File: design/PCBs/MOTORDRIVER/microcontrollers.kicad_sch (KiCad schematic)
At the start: 19 parts, among them IC1 ATSAME53J18A-MF, U11 ATSAMD11D14A-M

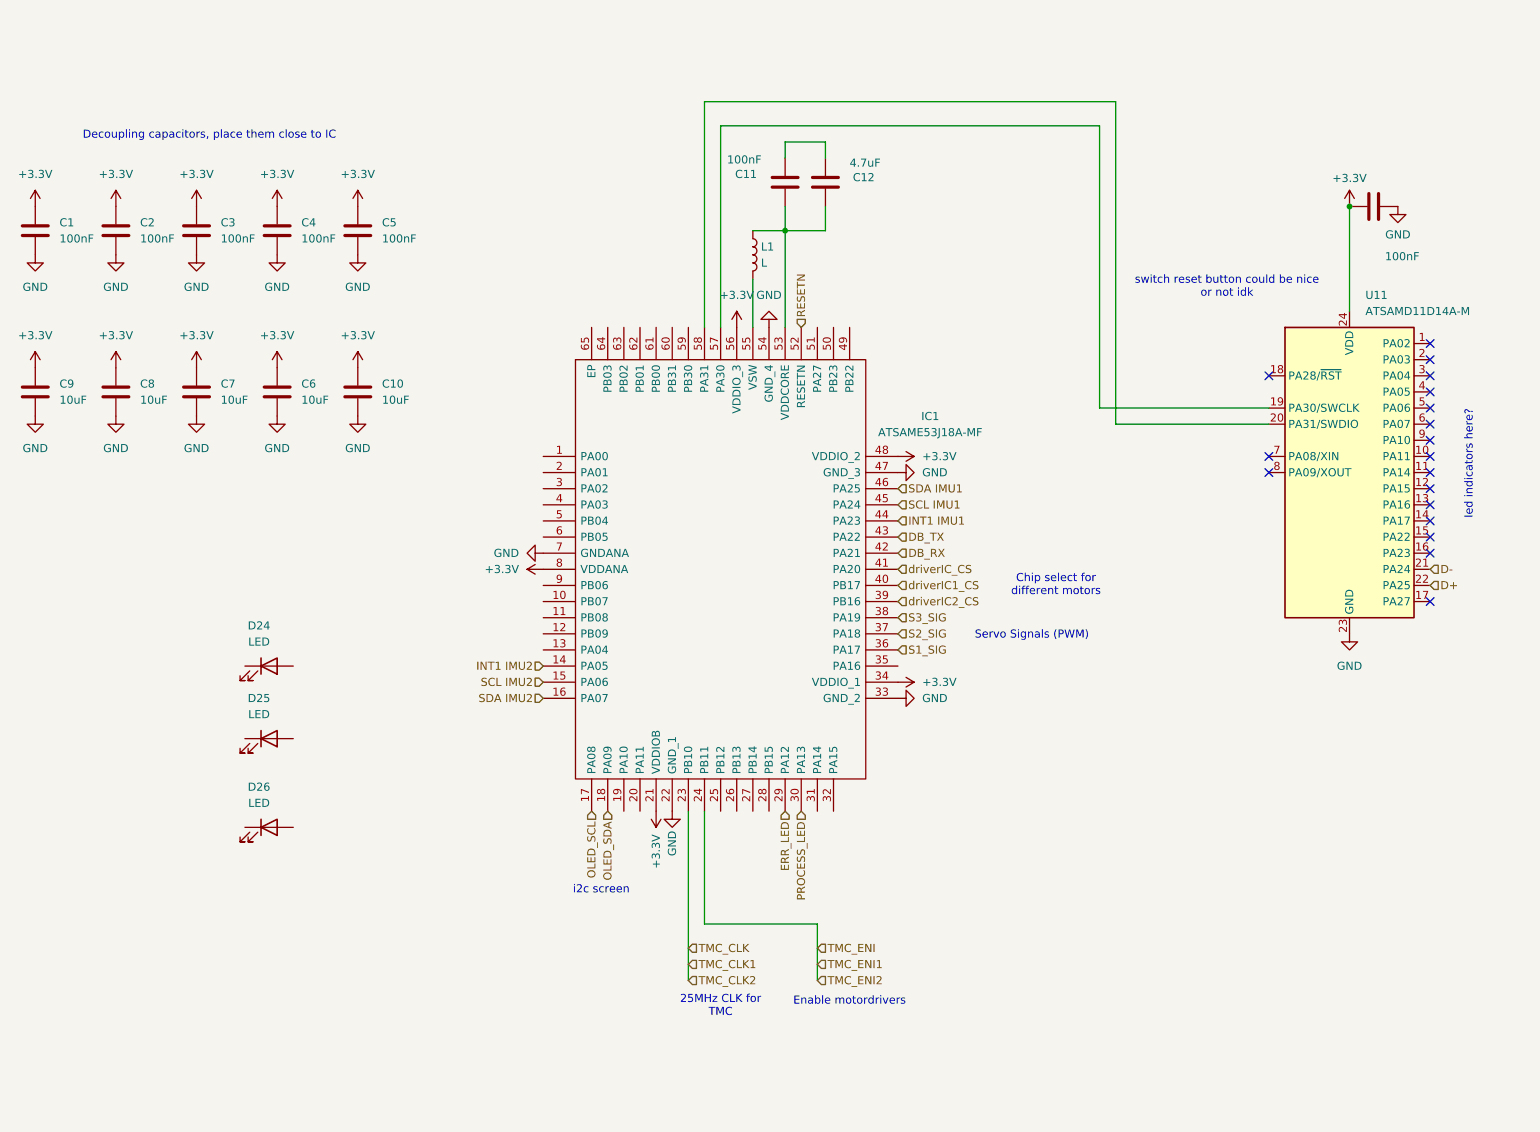
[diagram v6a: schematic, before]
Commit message: documentation, values, double-checking stuff
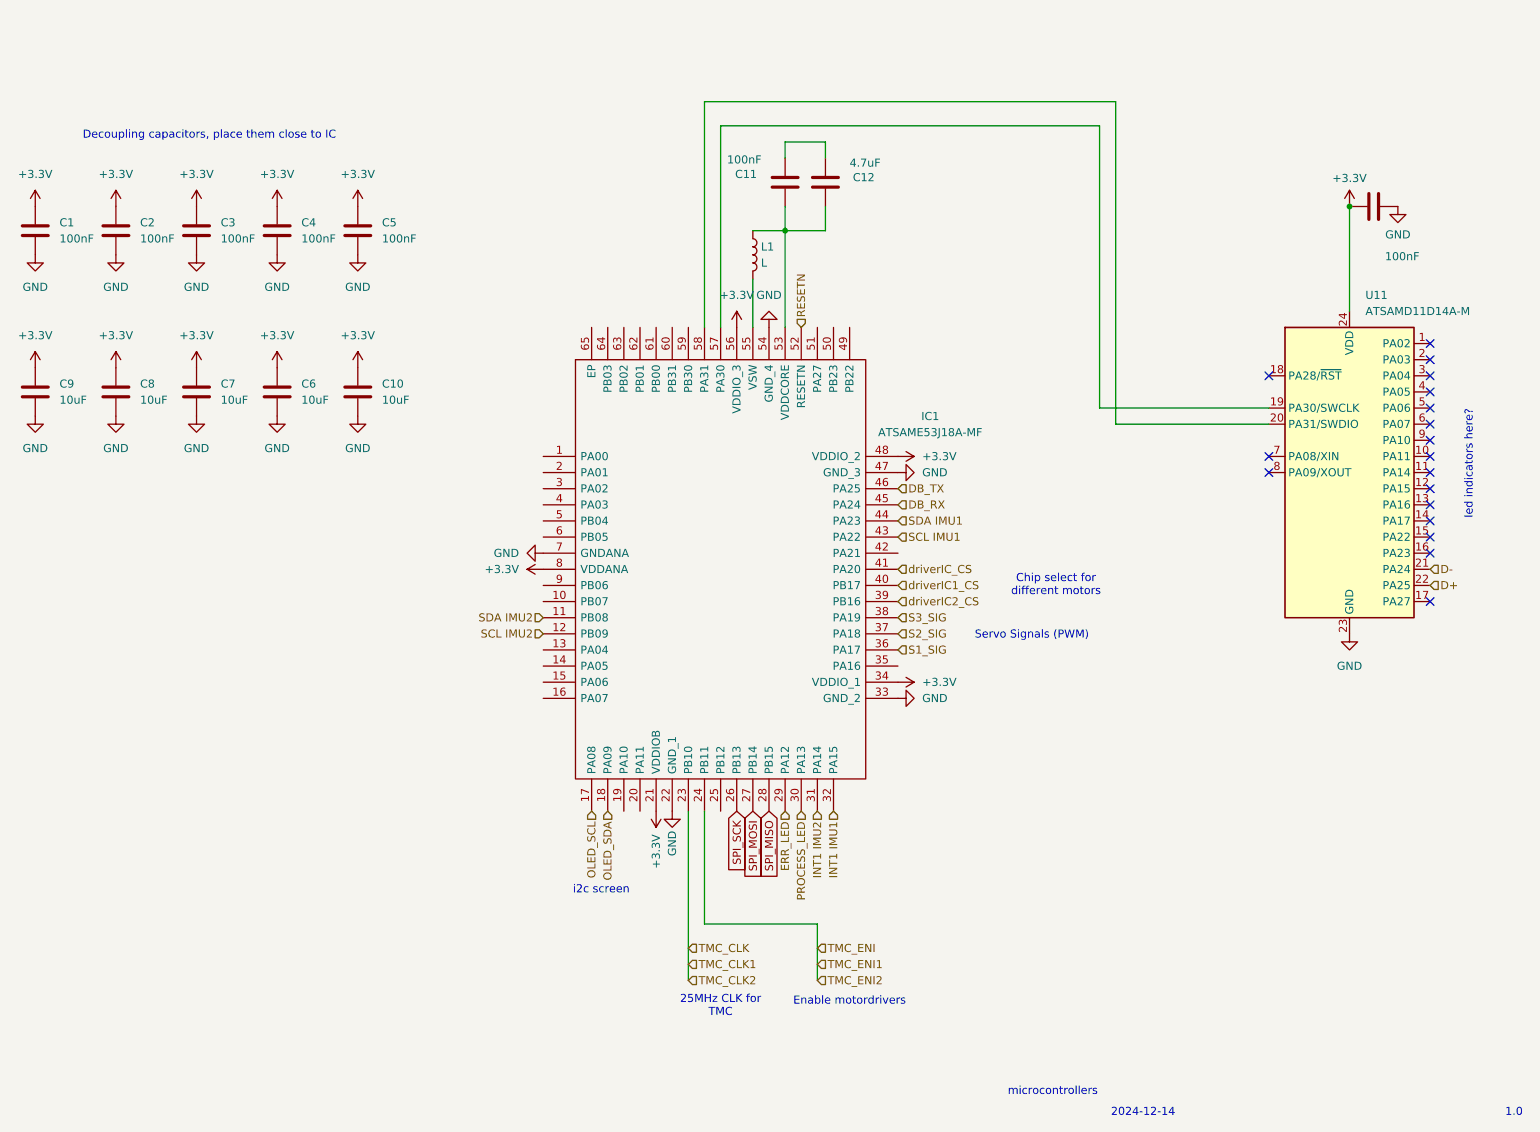
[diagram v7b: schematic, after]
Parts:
- removed D24, D25, D26: LED, symbol Device:LED
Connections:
- net DB_RX: now also IC1.45 (PA24); no longer IC1.42 (PA21)
- net DB_TX: now also IC1.46 (PA25); no longer IC1.43 (PA22)
- net INT1 IMU1: now also IC1.32 (PA15); no longer IC1.44 (PA23)
- net INT1 IMU2: now also IC1.31 (PA14); no longer IC1.14 (PA05)
- net SCL IMU1: now also IC1.43 (PA22); no longer IC1.45 (PA24)
- net SCL IMU2: now also IC1.12 (PB09); no longer IC1.15 (PA06)
- net SDA IMU1: now also IC1.44 (PA23); no longer IC1.46 (PA25)
- net SDA IMU2: now also IC1.11 (PB08); no longer IC1.16 (PA07)
- net SPI_SCK: now reaches IC1.26 (PB13)
- net SPI_MOSI: now reaches IC1.27 (PB14)
- net SPI_MISO: now reaches IC1.28 (PB15)
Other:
- note added: "1.0"
- note added: "2024-12-14"
- note added: "microcontrollers"
- note removed: "switch reset button could be nice or not idk"
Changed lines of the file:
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@@
 		)
 	)
+	(text "1.0"
+		(exclude_from_sim no)
+		(at 271.018 193.548 0)
+		(effects
+			(font
+				(size 1.27 1.27)
+			)
+		)
+	)
 	(text "Chip select for\ndifferent motors\n"
 		(exclude_from_sim no)
@@
 		)
 	)
-	(text "i2c screen"
+	(text "microcontrollers\n"
 		(exclude_from_sim no)
-		(at 127.254 158.496 0)
+		(at 198.374 190.246 0)
 		(effects
 			(font
@@
 		)
 	)
-	(text "switch reset button could be nice\nor not idk\n"
+	(text "i2c screen"
 		(exclude_from_sim no)
-		(at 225.806 63.5 0)
+		(at 127.254 158.496 0)
 		(effects
 			(font
@@
 		)
 	)
+	(text "2024-12-14"
+		(exclude_from_sim no)
+		(at 212.598 193.548 0)
+		(effects
+			(font
+				(size 1.27 1.27)
+			)
+		)
+	)
 	(text "Enable motordrivers"
 		(exclude_from_sim no)
@@
 		)
 	)
+	(global_label "SPI_MISO"
+		(shape input)
+		(at 153.67 146.05 270)
+		(fields_autoplaced yes)
+		(effects
+			(font
+				(size 1.27 1.27)
+			)
+			(justify right)
+		)
+		(property "Intersheetrefs" "${INTERSHEET_REFS}"
+			(at 153.67 157.3491 90)
+			(effects
+				(font
+					(size 1.27 1.27)
+				)
+				(justify right)
+				(hide yes)
+			)
+		)
+	)
+	(global_label "SPI_SCK"
+		(shape input)
+		(at 148.59 146.05 270)
+		(fields_autoplaced yes)
+		(effects
+			(font
+				(size 1.27 1.27)
+			)
+			(justify right)
+		)
+		(property "Intersheetrefs" "${INTERSHEET_REFS}"
+			(at 148.59 156.2821 90)
+			(effects
+				(font
+					(size 1.27 1.27)
+				)
+				(justify right)
+				(hide yes)
+			)
+		)
+	)
+	(global_label "SPI_MOSI"
+		(shape input)
+		(at 151.13 146.05 270)
+		(fields_autoplaced yes)
+		(effects
+			(font
+				(size 1.27 1.27)
+			)
+			(justify right)
+		)
+		(property "Intersheetrefs" "${INTERSHEET_REFS}"
+			(at 151.13 157.3491 90)
+			(effects
+				(font
+					(size 1.27 1.27)
+				)
+				(justify right)
+				(hide yes)
+			)
+		)
+	)
 	(hierarchical_label "driverIC2_CS"
 		(shape input)
@@
 	(hierarchical_label "SDA IMU1"
 		(shape input)
-		(at 173.99 95.25 0)
+		(at 173.99 100.33 0)
 		(fields_autoplaced yes)
 		(effects
@@
 	(hierarchical_label "DB_RX"
 		(shape input)
-		(at 173.99 105.41 0)
+		(at 173.99 97.79 0)
 		(fields_autoplaced yes)
 		(effects
@@
 	(hierarchical_label "DB_TX"
 		(shape input)
-		(at 173.99 102.87 0)
+		(at 173.99 95.25 0)
 		(fields_autoplaced yes)
 		(effects
@@
 	(hierarchical_label "SDA IMU2"
 		(shape input)
-		(at 118.11 128.27 180)
+		(at 118.11 115.57 180)
 		(fields_autoplaced yes)
 		(effects
@@
 	(hierarchical_label "SCL IMU2"
 		(shape input)
-		(at 118.11 125.73 180)
+		(at 118.11 118.11 180)
 		(fields_autoplaced yes)
 		(effects
@@
 	(hierarchical_label "SCL IMU1"
 		(shape input)
-		(at 173.99 97.79 0)
+		(at 173.99 102.87 0)
 		(fields_autoplaced yes)
 		(effects
@@
 	(hierarchical_label "INT1 IMU2"
 		(shape input)
-		(at 118.11 123.19 180)
+		(at 161.29 146.05 270)
 		(fields_autoplaced yes)
 		(effects
@@
 	(hierarchical_label "INT1 IMU1"
 		(shape input)
-		(at 173.99 100.33 0)
+		(at 163.83 146.05 270)
 		(fields_autoplaced yes)
 		(effects
@@
 				(size 1.27 1.27)
 			)
-			(justify left)
+			(justify right)
 		)
 	)
@@
 	)
 	(symbol
-		(lib_id "Device:LED")
-		(at 74.93 148.59 0)
-		(unit 1)
-		(exclude_from_sim no)
-		(in_bom yes)
-		(on_board yes)
-		(dnp no)
-		(fields_autoplaced yes)
-		(property "Reference" "D26"
-			(at 73.3425 142.24 0)
-			(effects
-				(font
-					(size 1.27 1.27)
-				)
-			)
-		)
-		(property "Value" "LED"
-			(at 73.3425 144.78 0)
-			(effects
-				(font
-					(size 1.27 1.27)
-				)
-			)
-		)
-		(property "Footprint" ""
-			(at 74.93 148.59 0)
-			(effects
-				(font
-					(size 1.27 1.27)
-				)
-				(hide yes)
-			)
-		)
-		(property "Datasheet" "~"
-			(at 74.93 148.59 0)
-			(effects
-				(font
-					(size 1.27 1.27)
-				)
-				(hide yes)
-			)
-		)
-		(property "Description" "Light emitting diode"
-			(at 74.93 148.59 0)
-			(effects
-				(font
-					(size 1.27 1.27)
-				)
-				(hide yes)
-			)
-		)
-		(pin "1"
-		)
-		(pin "2"
-		)
-		(instances
-			(project "motordriver"
-				(path "/c7634e88-16d1-45ec-9aac-9c841e03cf6d/9ebbb593-eaf1-4a56-ba2a-164e20b1d55e"
-					(reference "D26")
-					(unit 1)
-				)
-			)
-		)
-	)
-	(symbol
 		(lib_id "power:GND")
 		(at 63.5 83.82 0)
@@
 	)
 	(symbol
-		(lib_id "Device:LED")
-		(at 74.93 134.62 0)
-		(unit 1)
-		(exclude_from_sim no)
-		(in_bom yes)
-		(on_board yes)
-		(dnp no)
-		(fields_autoplaced yes)
-		(property "Reference" "D25"
-			(at 73.3425 128.27 0)
-			(effects
-				(font
-					(size 1.27 1.27)
-				)
-			)
-		)
-		(property "Value" "LED"
-			(at 73.3425 130.81 0)
-			(effects
-				(font
-					(size 1.27 1.27)
-				)
-			)
-		)
-		(property "Footprint" ""
-			(at 74.93 134.62 0)
-			(effects
-				(font
-					(size 1.27 1.27)
-				)
-				(hide yes)
-			)
-		)
-		(property "Datasheet" "~"
-			(at 74.93 134.62 0)
-			(effects
-				(font
-					(size 1.27 1.27)
-				)
-				(hide yes)
-			)
-		)
-		(property "Description" "Light emitting diode"
-			(at 74.93 134.62 0)
-			(effects
-				(font
-					(size 1.27 1.27)
-				)
-				(hide yes)
-			)
-		)
-		(pin "1"
-		)
-		(pin "2"
-		)
-		(instances
-			(project "motordriver"
-				(path "/c7634e88-16d1-45ec-9aac-9c841e03cf6d/9ebbb593-eaf1-4a56-ba2a-164e20b1d55e"
-					(reference "D25")
-					(unit 1)
-				)
-			)
-		)
-	)
-	(symbol
 		(lib_id "power:+3.3V")
 		(at 76.2 50.8 0)
@@
 					(unit 1)
 				)
-			)
-		)
-	)
-	(symbol
-		(lib_id "Device:LED")
-		(at 74.93 123.19 0)
-		(unit 1)
-		(exclude_from_sim no)
-		(in_bom yes)
-		(on_board yes)
-		(dnp no)
-		(fields_autoplaced yes)
-		(property "Reference" "D24"
-			(at 73.3425 116.84 0)
-			(effects
-				(font
-					(size 1.27 1.27)
-				)
-			)
-		)
-		(property "Value" "LED"
-			(at 73.3425 119.38 0)
-			(effects
-				(font
-					(size 1.27 1.27)
-				)
-			)
-		)
-		(property "Footprint" ""
-			(at 74.93 123.19 0)
-			(effects
-				(font
-					(size 1.27 1.27)
-				)
-				(hide yes)
-			)
-		)
-		(property "Datasheet" "~"
-			(at 74.93 123.19 0)
-			(effects
-				(font
-					(size 1.27 1.27)
-				)
-				(hide yes)
-			)
-		)
-		(property "Description" "Light emitting diode"
-			(at 74.93 123.19 0)
-			(effects
-				(font
-					(size 1.27 1.27)
-				)
-				(hide yes)
-			)
-		)
-		(pin "1"
-		)
-		(pin "2"
-		)
-		(instances
-			(project ""
-				(path "/c7634e88-16d1-45ec-9aac-9c841e03cf6d/9ebbb593-eaf1-4a56-ba2a-164e20b1d55e"
-					(reference "D24")
-					(unit 1)
-				)

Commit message: cleaned up, added values and footprints
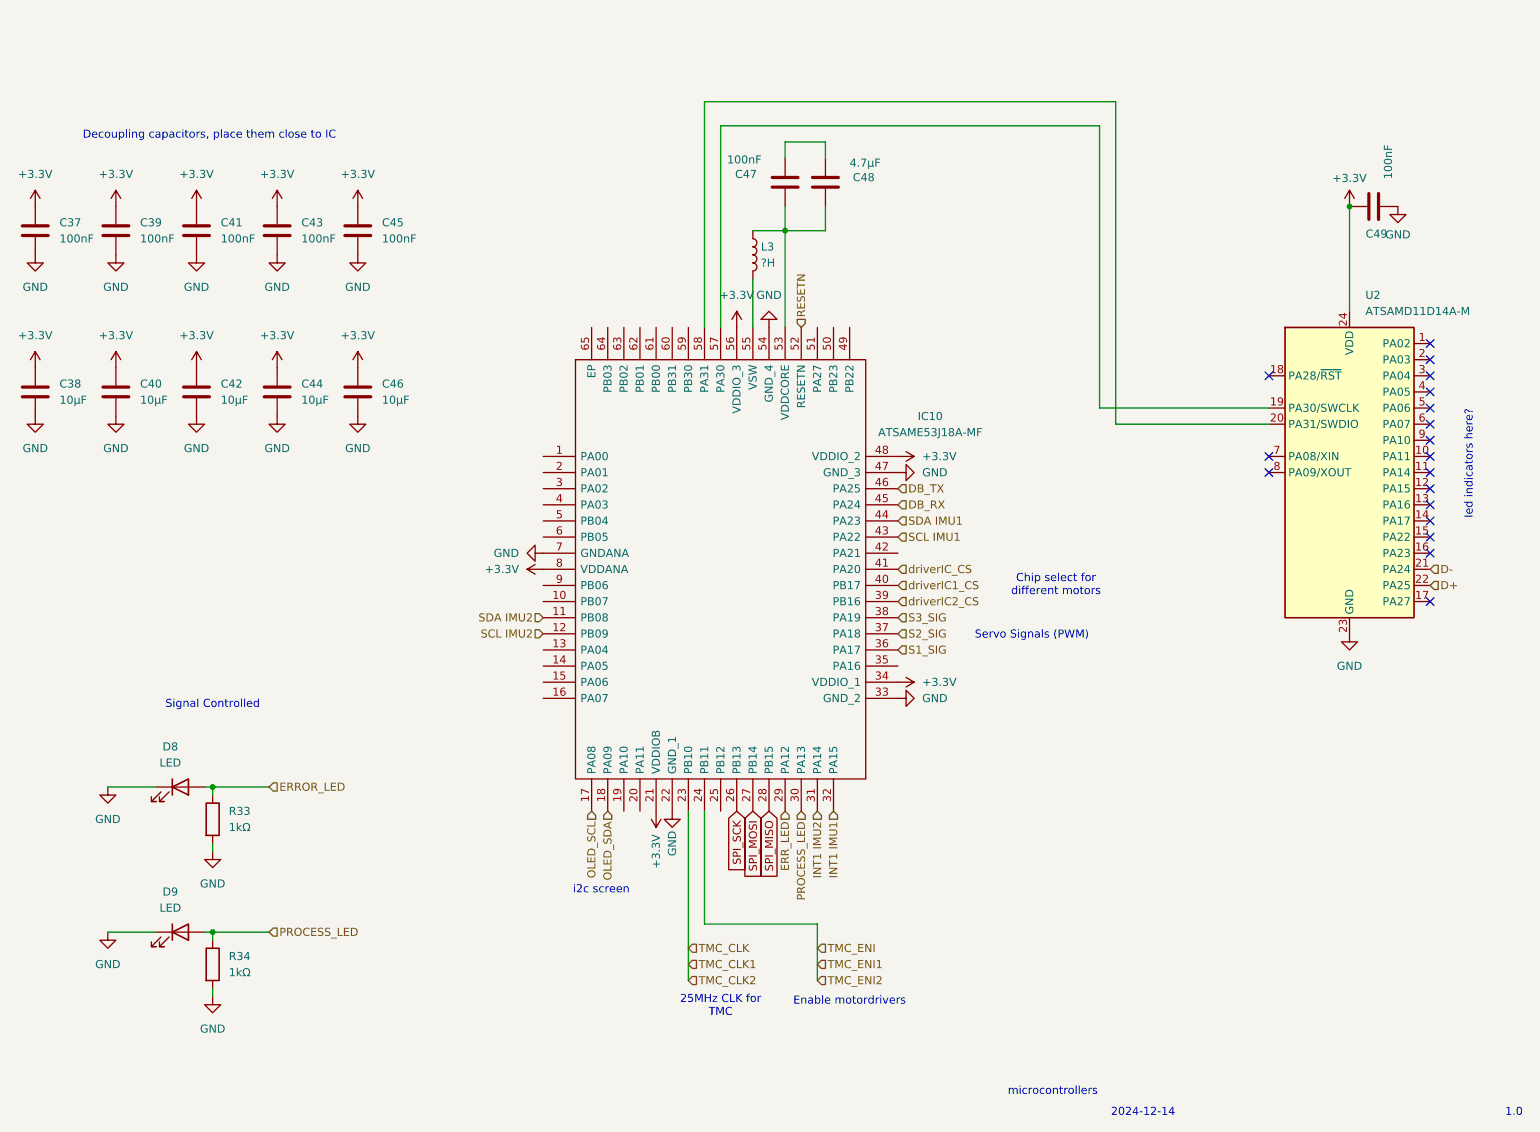
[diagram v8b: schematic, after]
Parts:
- added D8, D9: LED, Diode_SMD:D_0603_1608Metric, symbol Device:LED
- added R33, R34: 1kΩ, Resistor_SMD:R_0603_1608Metric, symbol Device:R
- C37: renamed from C1; footprint (none) -> Capacitor_SMD:C_0603_1608Metric
- C38: renamed from C9; value 10uF -> 10µF; footprint (none) -> Capacitor_SMD:C_0603_1608Metric
- C39: renamed from C2; footprint (none) -> Capacitor_SMD:C_0603_1608Metric
- C40: renamed from C8; value 10uF -> 10µF; footprint (none) -> Capacitor_SMD:C_0603_1608Metric
- C41: renamed from C3; footprint (none) -> Capacitor_SMD:C_0603_1608Metric
- C42: renamed from C7; value 10uF -> 10µF; footprint (none) -> Capacitor_SMD:C_0603_1608Metric
- C43: renamed from C4; footprint (none) -> Capacitor_SMD:C_0603_1608Metric
- C44: renamed from C6; value 10uF -> 10µF; footprint (none) -> Capacitor_SMD:C_0603_1608Metric
- C45: renamed from C5; footprint (none) -> Capacitor_SMD:C_0603_1608Metric
- C46: renamed from C10; value 10uF -> 10µF; footprint (none) -> Capacitor_SMD:C_0603_1608Metric
- C47: renamed from C11; footprint (none) -> Capacitor_SMD:C_0603_1608Metric
- C48: renamed from C12; value 4.7uF -> 4.7µF; footprint (none) -> Capacitor_SMD:C_0603_1608Metric
- C49: renamed from 100nF; value C -> 100nF; footprint (none) -> Capacitor_SMD:C_0603_1608Metric
- L3: renamed from L1; value L -> ?H; footprint (none) -> Inductor_SMD:L_0603_1608Metric
- renumbered IC1 to IC10, U11 to U2
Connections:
- net GND: now also D8.1 (K), D9.1 (K), R33.2, R34.2
- net PROCESS_LED: now also D9.2 (A), R34.1
- new net ERROR_LED: D8.2 (A), R33.1
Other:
- note added: "Signal Controlled"
